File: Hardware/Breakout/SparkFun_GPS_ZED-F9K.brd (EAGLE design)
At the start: 43.2 x 43.2 mm, 126 parts, among them J1 U.FL, J3 QWIIC_RIGHT_ANGLE, J4 QWIIC_RIGHT_ANGLE, U1 UBLOX_ZED_F9R, U2 3.3V

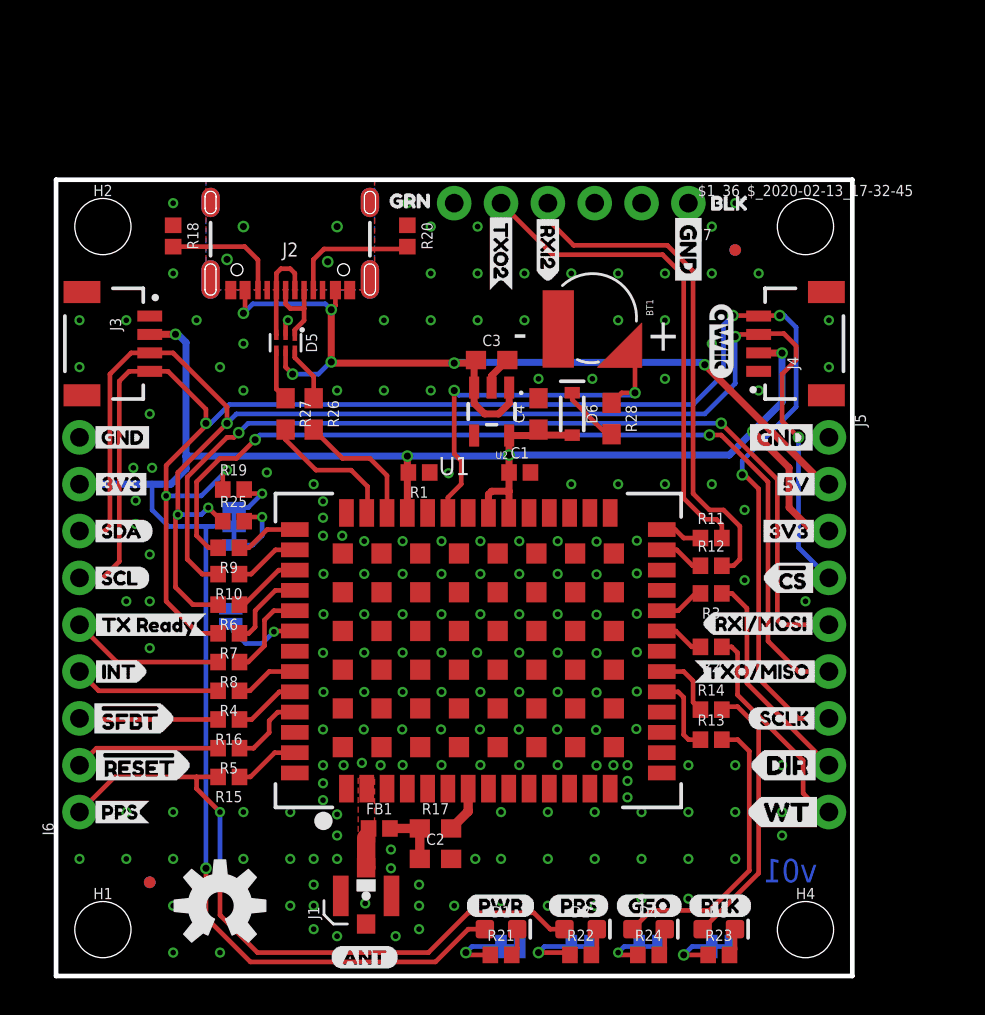
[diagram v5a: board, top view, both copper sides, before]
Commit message: Adds automotive certified diode to wt/dir circuitry
* Adds wt/dir circuitry to both breakout board and pi hat
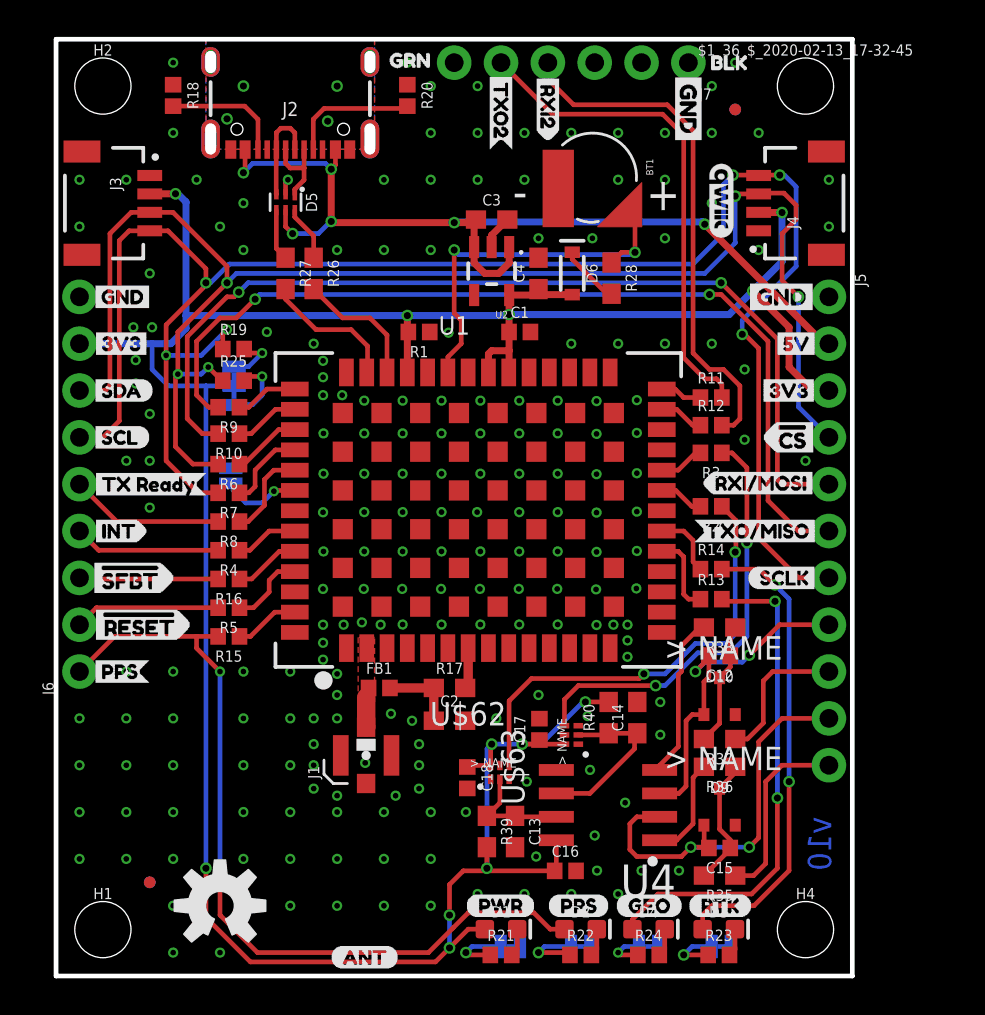
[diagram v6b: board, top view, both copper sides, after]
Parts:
- removed U$10: (no value), wt_dir:DIR1
- removed U$13: (no value), wt_dir:WT0
- removed U$32: (no value), wt_dir:DIR3
- removed U$50: (no value), wt_dir:WT2
- added C12, C15: 1.0nF, SparkFun-Capacitors:0402
- added C13, C14: 22nF, SparkFun-Capacitors:0603
- added C16, C17, C18: 0.1uF, SparkFun-Capacitors:0402
- added D10, D9: 0.5A/40V/420mV, classified:SOT23_BZX
- added R35, R37: 3.3k, SparkFun-Resistors:0603
- added R36, R38: 470, SparkFun-Resistors:0603
- added R39, R40: 910, classified:0603
- added U$62, U$63: UHS_INVERTER_SCHMITT_TRIGGERSIP6, classified:SIP6
- added U4: HCPL-270L, classified:SOP_8-PIN
- J2: device SparkFun-Connectors:USB-C-16P -> SparkFun-Connectors:USB-C-16P-2LAYER-PADS
- J5: device SparkFun-Connectors:1X09_NO_SILK -> SparkFun-Connectors:1X11_NO_SILK
- moved R17 7.66 mm to (21.3, 15.6)
- moved BT1 7.62 mm to (29.1, 43.3)
- moved FD3 7.62 mm to (36.8, 47.0)
- moved FD4 7.62 mm to (36.8, 47.0)
- moved J7 7.62 mm to (34.3, 49.5)
- moved R18 7.62 mm to (6.35, 47.8)
- moved R20 7.62 mm to (19.1, 47.8)
- moved U$21 7.62 mm to (34.8, 49.5)
- moved U$54 7.62 mm to (38.1, 49.5)
- moved C4 7.62 mm to (26.2, 38.1)
- moved D6 7.62 mm to (28.0, 38.1)
- moved FB1 7.62 mm to (17.5, 15.6)
- moved J6 7.62 mm to (1.27, 16.5)
- moved R10 7.62 mm to (9.37, 29.4)
- moved R12 7.62 mm to (35.5, 29.9)
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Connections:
- removed net DIR: J5.8, R3.1
- removed net WT: J5.9, R2.1
- new net DIR+: J5.9, R37.1
- new net DIR-: C12.2, D10.P1, J5.8, U4.P3
- new net DIR_IN: R38.2, U4.P4
- new net DIR_OUT: R3.1, U$63.P4
- new net DIR_SCHMITT: C14.1, R40.1, U$63.P2, U4.P6
- new net N$35: C15.1, D9.P3, R35.2, R36.1
- new net N$37: C12.1, D10.P3, R37.2, R38.1
- new net WT+: J5.11, R35.1
- new net WT-: C15.2, D9.P1, J5.10, U4.P2
- new net WT_IN: R36.2, U4.P1
- new net WT_OUT: R2.1, U$62.P4
- new net WT_SCHMITT: C13.1, R39.1, U$62.P2, U4.P7
- net 3.3V: now also C16.1, C17.1, C18.1, R39.2, R40.2, U$62.P6, U$63.P6, U4.P8
- net GND: now also C13.2, C14.2, C16.2, C17.2, C18.2, U$62.P3, U$63.P3, U4.P5
- net SHIELD: no longer J2.SHLD5, J2.SHLD6, J2.SHLD7, J2.SHLD8
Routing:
- net 3.3V: track 117.7 -> 157.1 mm, vias 6 -> 12
- net WT_OUT: track 0.00 -> 24.5 mm, vias 0 -> 2
- net DIR_OUT: track 0.00 -> 23.6 mm, vias 0 -> 2
- net WT-: track 0.00 -> 22.6 mm, vias 0 -> 2
- net DIR-: track 0.00 -> 19.0 mm, vias 0 -> 2
- net DIR: track 12.0 -> 0.00 mm
- net WT: track 11.9 -> 0.00 mm
- net GEOF_STAT: track 15.9 -> 27.0 mm, vias 0 -> 2
- net RTK_STAT: track 14.7 -> 25.5 mm, vias 0 -> 2
- net WT+: track 0.00 -> 10.2 mm
- net DIR_SCHMITT: track 0.00 -> 9.38 mm
- net DIR_IN: track 0.00 -> 8.86 mm
- net DIR+: track 0.00 -> 7.93 mm
- net PPS: track 37.1 -> 44.7 mm
- net N$35: track 0.00 -> 7.09 mm
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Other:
- board size 43.2 x 43.2 mm -> 43.2 x 50.8 mm
- board text added: "v10"
- board text removed: "v01"

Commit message: Adds labels for new PTH for wt/dir lines
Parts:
- added U$10: (no value), WT_dir_small:D#0
- added U$13: (no value), WT_dir_small:D#1
- added U$32: (no value), WT_dir_small:W#2
- added U$50: (no value), WT_dir_small:W#3
- added U$60: (no value), wt_dir:D#0
- added U$61: (no value), wt_dir:D#1
- added U$64: (no value), wt_dir:W#2
- added U$65: (no value), wt_dir:W#3
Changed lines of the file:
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@@
 <layer number="19" name="Unrouted" color="6" fill="1" visible="yes" active="yes"/>
 <layer number="20" name="Dimension" color="15" fill="1" visible="yes" active="yes"/>
-<layer number="21" name="tPlace" color="16" fill="1" visible="no" active="yes"/>
-<layer number="22" name="bPlace" color="14" fill="1" visible="no" active="yes"/>
+<layer number="21" name="tPlace" color="16" fill="1" visible="yes" active="yes"/>
+<layer number="22" name="bPlace" color="14" fill="1" visible="yes" active="yes"/>
 <layer number="23" name="tOrigins" color="15" fill="1" visible="yes" active="yes"/>
 <layer number="24" name="bOrigins" color="15" fill="1" visible="yes" active="yes"/>
@@
 <layer number="37" name="tTest" color="7" fill="1" visible="no" active="yes"/>
 <layer number="38" name="bTest" color="7" fill="1" visible="no" active="yes"/>
-<layer number="39" name="tKeepout" color="4" fill="11" visible="yes" active="yes"/>
+<layer number="39" name="tKeepout" color="4" fill="11" visible="no" active="yes"/>
 <layer number="40" name="bKeepout" color="1" fill="11" visible="no" active="yes"/>
 <layer number="41" name="tRestrict" color="4" fill="10" visible="no" active="yes"/>
@@
 <layer number="45" name="Holes" color="7" fill="1" visible="yes" active="yes"/>
 <layer number="46" name="Milling" color="3" fill="1" visible="no" active="yes"/>
-<layer number="47" name="Measures" color="7" fill="1" visible="yes" active="yes"/>
+<layer number="47" name="Measures" color="7" fill="1" visible="no" active="yes"/>
 <layer number="48" name="Document" color="7" fill="1" visible="no" active="yes"/>
 <layer number="49" name="Reference" color="13" fill="1" visible="yes" active="yes"/>
@@
 <layer number="115" name="ReferenceISLANDS" color="7" fill="1" visible="no" active="no"/>
 <layer number="116" name="Patch_BOT" color="9" fill="4" visible="no" active="no"/>
-<layer number="117" name="PM_Ref" color="26" fill="1" visible="yes" active="yes"/>
+<layer number="117" name="PM_Ref" color="26" fill="1" visible="no" active="yes"/>
 <layer number="118" name="Rect_Pads" color="7" fill="1" visible="no" active="no"/>
-<layer number="119" name="PF_Ref" color="31" fill="1" visible="yes" active="yes"/>
-<layer number="120" name="WFL_Ref" color="25" fill="1" visible="yes" active="yes"/>
+<layer number="119" name="PF_Ref" color="31" fill="1" visible="no" active="yes"/>
+<layer number="120" name="WFL_Ref" color="25" fill="1" visible="no" active="yes"/>
 <layer number="121" name="_tsilk" color="7" fill="1" visible="no" active="no"/>
 <layer number="122" name="_bsilk" color="7" fill="1" visible="no" active="no"/>
@@
 <attribute name="VALUE" x="21.539" y="10.754" size="0.6096" layer="27" font="vector" ratio="20" rot="R270" align="top-center"/>
 </element>
+<element name="U$10" library="WT_dir_small" package="D#0" value="" x="38.735" y="16.51" smashed="yes"/>
+<element name="U$13" library="WT_dir_small" package="D#1" value="" x="38.862" y="19.05" smashed="yes"/>
+<element name="U$32" library="WT_dir_small" package="W#2" value="" x="38.481" y="11.43" smashed="yes"/>
+<element name="U$50" library="WT_dir_small" package="W#3" value="" x="38.608" y="13.97" smashed="yes"/>
+<element name="U$60" library="wt_dir" package="D#0" value="" x="38.1" y="18.923" smashed="yes" rot="MR180"/>
+<element name="U$61" library="wt_dir" package="D#1" value="" x="38.227" y="16.51" smashed="yes" rot="MR180"/>
+<element name="U$64" library="wt_dir" package="W#2" value="" x="37.719" y="11.43" smashed="yes" rot="MR180"/>
+<element name="U$65" library="wt_dir" package="W#3" value="" x="37.846" y="13.97" smashed="yes" rot="MR180"/>
 </elements>
 <signals>

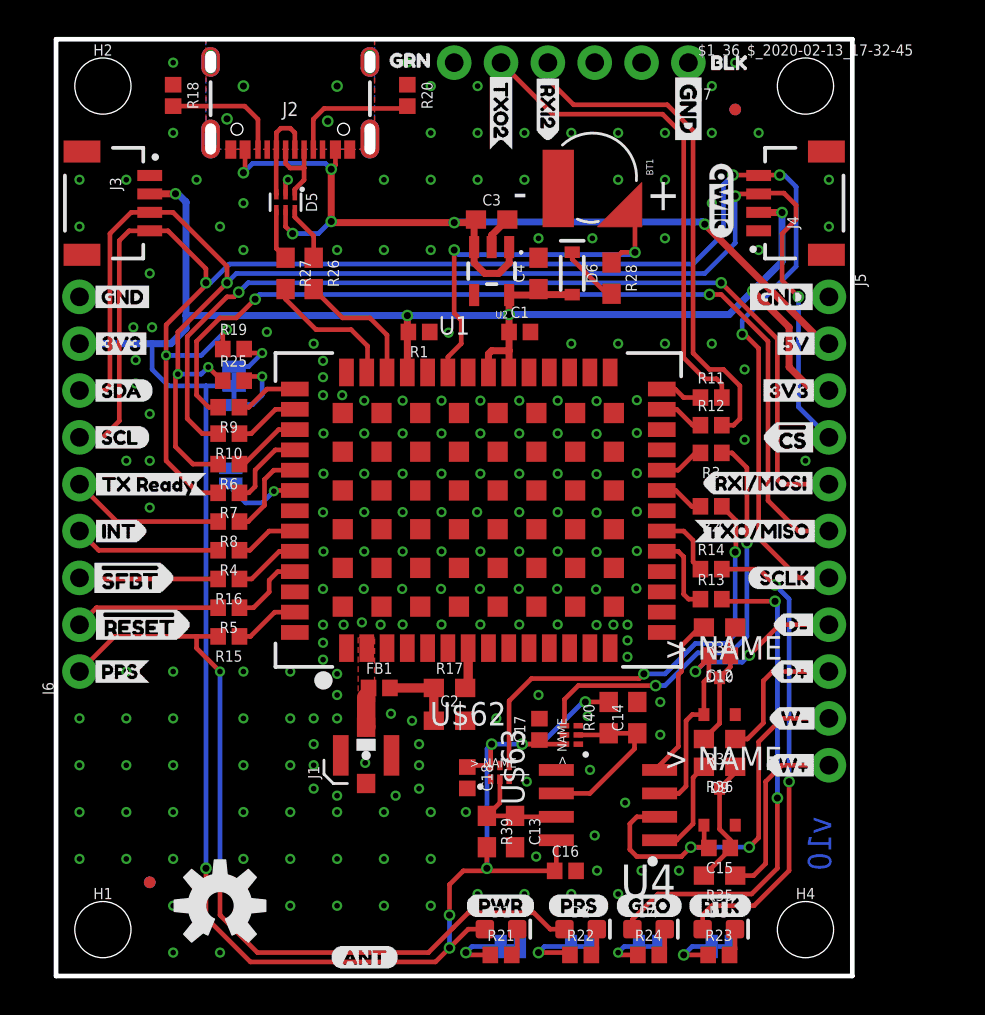
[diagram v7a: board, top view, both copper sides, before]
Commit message: Updates designs with new X7R capacitors
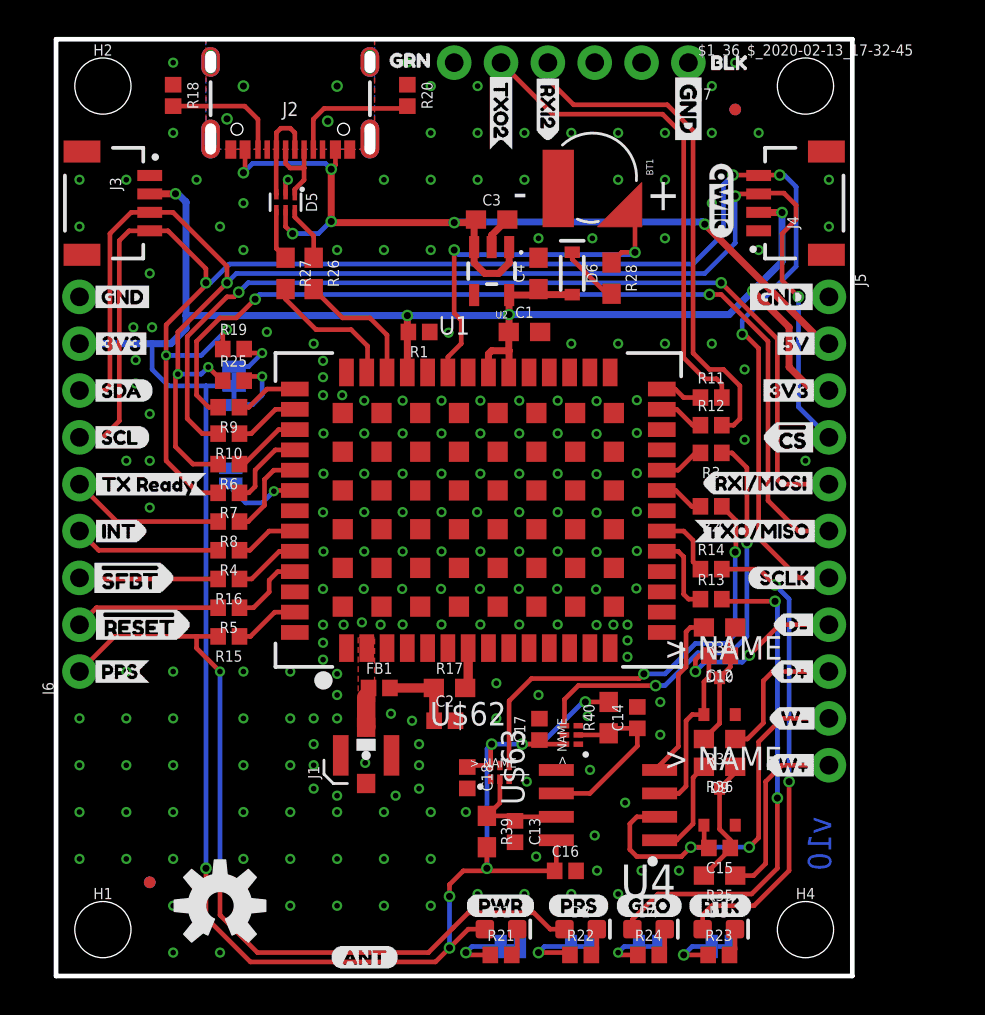
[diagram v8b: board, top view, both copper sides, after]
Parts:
- C1: device SparkFun-Capacitors:0402 -> SparkFun-Capacitors:0603
- C12, C15: value 1.0nF -> 1nF
- C13, C14, C2: device SparkFun-Capacitors:0603 -> SparkFun-Capacitors:0402
- moved C1 0.25 mm to (25.4, 34.9)
- moved C2 0.25 mm to (21.1, 13.8)
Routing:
- net GND: vias 202 -> 203
